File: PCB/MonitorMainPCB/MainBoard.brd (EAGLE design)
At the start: 94.1 x 100 mm, 147 parts, among them IC1 ADS1293, IC2 LP3878MR-ADJ_NOPB, J1 POWER_JACK, J2 USB_B_PTH, J6 2X6 FEMALE, U2 TPS7A4901DGNR, U3 AFE4400_RHA_40, U4 MSP430F149IPAG, Y1 4.096MHz, Y2 8MHz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

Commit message: update some kind of mianPCB
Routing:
- net PD_ALM: track 80.9 -> 79.0 mm
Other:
- board text added: "ADS"
- board text added: "AFE"
- board text added: "BT"
- board text added: "HR"
- board text added: "MSP"
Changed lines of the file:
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@@
 <setting verticaltext="up"/>
 </settings>
-<grid distance="10" unitdist="mil" unit="mil" style="lines" multiple="1" display="yes" altdistance="5" altunitdist="mil" altunit="mil"/>
+<grid distance="5" unitdist="mil" unit="mil" style="lines" multiple="1" display="yes" altdistance="5" altunitdist="mil" altunit="mil"/>
 <layers>
 <layer number="1" name="Top" color="4" fill="1" visible="yes" active="yes"/>
@@
 <text x="26.6192" y="19.9644" size="1.016" layer="25" font="vector" ratio="20">U1</text>
 <text x="49.7332" y="60.3504" size="1.016" layer="21" font="vector" ratio="20">U5</text>
+<text x="85.852" y="70.993" size="1.016" layer="21" font="vector" ratio="20">ADS</text>
+<text x="85.852" y="69.723" size="1.016" layer="21" font="vector" ratio="20">AFE</text>
+<text x="85.852" y="68.199" size="1.016" layer="21" font="vector" ratio="20">BT</text>
+<text x="85.852" y="66.802" size="1.016" layer="21" font="vector" ratio="20">HR</text>
+<text x="85.852" y="65.405" size="1.016" layer="21" font="vector" ratio="20">MSP</text>
 </plain>
 <attributes>
@@
 <wire x1="58.293" y1="62.1382125" x2="59.2652125" y2="61.166" width="0.254" layer="16"/>
 <wire x1="58.293" y1="74.207425" x2="58.293" y2="62.1382125" width="0.254" layer="16"/>
-<wire x1="86.0298" y1="66.04" x2="86.0806" y2="66.04" width="0.254" layer="16"/>
-<via x="86.0806" y="66.04" extent="1-16" drill="0.35"/>
-<wire x1="86.0806" y1="66.04" x2="86.0806" y2="67.2338" width="0.254" layer="1"/>
-<wire x1="86.0806" y1="67.2338" x2="86.0806" y2="67.3354" width="0.254" layer="1"/>
 <contactref element="U4" pad="37"/>
-<wire x1="86.0806" y1="67.2338" x2="84.4804" y2="68.834" width="0.254" layer="1"/>
-<wire x1="84.4804" y1="68.834" x2="79.7306" y2="68.834" width="0.254" layer="1"/>
 <wire x1="59.484" y1="61.166" x2="59.9214" y2="61.166" width="0.254" layer="16"/>
 <wire x1="59.9214" y1="61.166" x2="60.6298" y2="61.8744" width="0.254" layer="16"/>
@@
 <wire x1="64.3706125" y1="61.8518" x2="64.9153875" y2="61.8518" width="0.254" layer="16"/>
 <wire x1="64.9153875" y1="61.8518" x2="64.9379875" y2="61.8744" width="0.254" layer="16"/>
-<wire x1="81.8642" y1="61.8744" x2="86.0298" y2="66.04" width="0.254" layer="16"/>
 <wire x1="64.9379875" y1="61.8744" x2="81.8642" y2="61.8744" width="0.254" layer="16"/>
+<wire x1="81.8642" y1="61.8744" x2="84.836" y2="64.8462" width="0.254" layer="16"/>
+<via x="84.836" y="67.31" extent="1-16" drill="0.35"/>
+<wire x1="84.836" y1="64.8462" x2="84.836" y2="67.31" width="0.254" layer="16"/>
+<wire x1="79.7306" y1="68.834" x2="83.312" y2="68.834" width="0.254" layer="1"/>
+<wire x1="83.312" y1="68.834" x2="84.836" y2="67.31" width="0.254" layer="1"/>
 </signal>
 <signal name="ADC_RDY">
@@
 <wire x1="81.8642" y1="66.8274" x2="83.6422" y2="65.0494" width="0.254" layer="1"/>
 <wire x1="83.6422" y1="65.0494" x2="83.6422" y2="63.7286" width="0.254" layer="1"/>
-<wire x1="78.2066" y1="58.293" x2="83.6422" y2="63.7286" width="0.254" layer="1"/>
+<wire x1="78.2066" y1="58.293" x2="81.8388" y2="61.9252" width="0.254" layer="1"/>
+<wire x1="81.8388" y1="61.9252" x2="83.6422" y2="63.7286" width="0.254" layer="1"/>
 <wire x1="64.611125" y1="58.293" x2="67.4116" y2="58.293" width="0.254" layer="1"/>
 <contactref element="J7" pad="3"/>

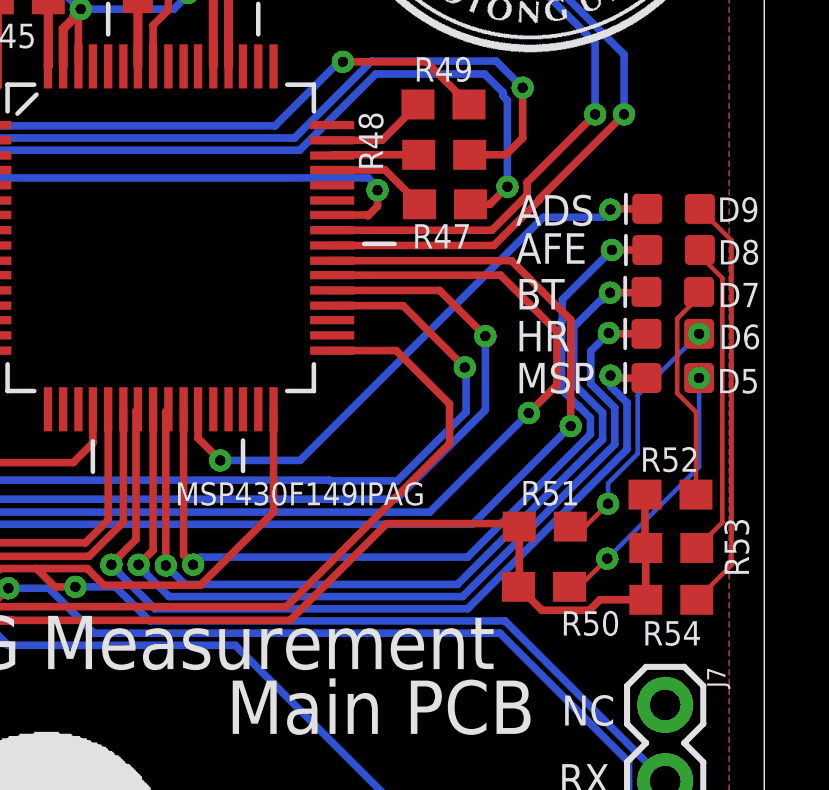
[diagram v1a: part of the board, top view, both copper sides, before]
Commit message: Revert "Merge branch 'master' of https://github.com/celelion/ECGMonitor"
This reverts commit f7783cc06e649bc8b4ab999284b80d95ebf74241, reversing
changes made to 6526a36a7f04e243d33003dbca553b52cb26d685.
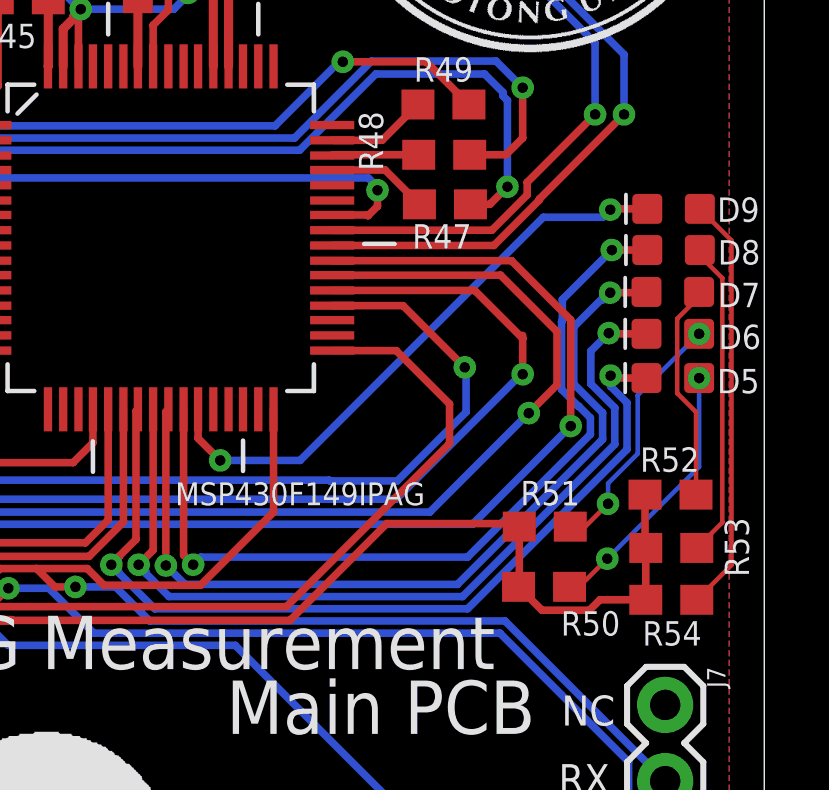
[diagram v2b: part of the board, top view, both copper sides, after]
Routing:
- net PD_ALM: track 79.0 -> 80.9 mm
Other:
- board text removed: "ADS"
- board text removed: "AFE"
- board text removed: "BT"
- board text removed: "HR"
- board text removed: "MSP"
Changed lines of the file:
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@@
 <setting verticaltext="up"/>
 </settings>
-<grid distance="5" unitdist="mil" unit="mil" style="lines" multiple="1" display="yes" altdistance="5" altunitdist="mil" altunit="mil"/>
+<grid distance="10" unitdist="mil" unit="mil" style="lines" multiple="1" display="yes" altdistance="5" altunitdist="mil" altunit="mil"/>
 <layers>
 <layer number="1" name="Top" color="4" fill="1" visible="yes" active="yes"/>
@@
 <text x="26.6192" y="19.9644" size="1.016" layer="25" font="vector" ratio="20">U1</text>
 <text x="49.7332" y="60.3504" size="1.016" layer="21" font="vector" ratio="20">U5</text>
-<text x="85.852" y="70.993" size="1.016" layer="21" font="vector" ratio="20">ADS</text>
-<text x="85.852" y="69.723" size="1.016" layer="21" font="vector" ratio="20">AFE</text>
-<text x="85.852" y="68.199" size="1.016" layer="21" font="vector" ratio="20">BT</text>
-<text x="85.852" y="66.802" size="1.016" layer="21" font="vector" ratio="20">HR</text>
-<text x="85.852" y="65.405" size="1.016" layer="21" font="vector" ratio="20">MSP</text>
 </plain>
 <attributes>
@@
 <wire x1="58.293" y1="62.1382125" x2="59.2652125" y2="61.166" width="0.254" layer="16"/>
 <wire x1="58.293" y1="74.207425" x2="58.293" y2="62.1382125" width="0.254" layer="16"/>
+<wire x1="86.0298" y1="66.04" x2="86.0806" y2="66.04" width="0.254" layer="16"/>
+<via x="86.0806" y="66.04" extent="1-16" drill="0.35"/>
+<wire x1="86.0806" y1="66.04" x2="86.0806" y2="67.2338" width="0.254" layer="1"/>
+<wire x1="86.0806" y1="67.2338" x2="86.0806" y2="67.3354" width="0.254" layer="1"/>
 <contactref element="U4" pad="37"/>
+<wire x1="86.0806" y1="67.2338" x2="84.4804" y2="68.834" width="0.254" layer="1"/>
+<wire x1="84.4804" y1="68.834" x2="79.7306" y2="68.834" width="0.254" layer="1"/>
 <wire x1="59.484" y1="61.166" x2="59.9214" y2="61.166" width="0.254" layer="16"/>
 <wire x1="59.9214" y1="61.166" x2="60.6298" y2="61.8744" width="0.254" layer="16"/>
@@
 <wire x1="64.3706125" y1="61.8518" x2="64.9153875" y2="61.8518" width="0.254" layer="16"/>
 <wire x1="64.9153875" y1="61.8518" x2="64.9379875" y2="61.8744" width="0.254" layer="16"/>
+<wire x1="81.8642" y1="61.8744" x2="86.0298" y2="66.04" width="0.254" layer="16"/>
 <wire x1="64.9379875" y1="61.8744" x2="81.8642" y2="61.8744" width="0.254" layer="16"/>
-<wire x1="81.8642" y1="61.8744" x2="84.836" y2="64.8462" width="0.254" layer="16"/>
-<via x="84.836" y="67.31" extent="1-16" drill="0.35"/>
-<wire x1="84.836" y1="64.8462" x2="84.836" y2="67.31" width="0.254" layer="16"/>
-<wire x1="79.7306" y1="68.834" x2="83.312" y2="68.834" width="0.254" layer="1"/>
-<wire x1="83.312" y1="68.834" x2="84.836" y2="67.31" width="0.254" layer="1"/>
 </signal>
 <signal name="ADC_RDY">
@@
 <wire x1="81.8642" y1="66.8274" x2="83.6422" y2="65.0494" width="0.254" layer="1"/>
 <wire x1="83.6422" y1="65.0494" x2="83.6422" y2="63.7286" width="0.254" layer="1"/>
-<wire x1="78.2066" y1="58.293" x2="81.8388" y2="61.9252" width="0.254" layer="1"/>
-<wire x1="81.8388" y1="61.9252" x2="83.6422" y2="63.7286" width="0.254" layer="1"/>
+<wire x1="78.2066" y1="58.293" x2="83.6422" y2="63.7286" width="0.254" layer="1"/>
 <wire x1="64.611125" y1="58.293" x2="67.4116" y2="58.293" width="0.254" layer="1"/>
 <contactref element="J7" pad="3"/>
